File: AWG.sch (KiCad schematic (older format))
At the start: 70 parts, among them J1 Conn Alimenation, J2 Conn afficheur, J3 Conn_01x04, J4 Conn_01x04, J5 SMA, J6 SMA, J7 BNC, Q1 Q_NPN_BCE, Q2 Q_PNP_BCE, SW1 Reset, SW2 Encodeur sur façade, SW3 Next, SW4 Previous, SW5 AC/DC, SW6 50R/Low Z, SW7 Next, SW8 Previous, U1 Pico, U2 L79L05_SOT89, U3 AD8055ARZ, U4 L78L05_SOT89

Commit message: new frontplate interface circuit, new power distrib
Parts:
- removed C1, C11, C2: 100n, Capacitor_SMD:C_0805_2012Metric_Pad1.18x1.45mm_HandSolder, symbol Device:C_Small
- removed C12, C8: 1u, symbol Device:CP_Small
- removed J1: Conn Alimenation, symbol Connector_Generic:Conn_01x04
- removed J3, J4: Conn_01x04, symbol Connector_Generic:Conn_01x04
- removed R1, R14, R15, R2, R3: 1k, Resistor_SMD:R_0805_2012Metric_Pad1.20x1.40mm_HandSolder, symbol Device:R_Small
- removed U2: L79L05_SOT89, Package_TO_SOT_SMD:SOT-89-3, symbol Regulator_Linear:L79L05_SOT89
- removed U4: L78L05_SOT89, Package_TO_SOT_SMD:SOT-89-3, symbol Regulator_Linear:L78L05_SOT89
- added C? (x4): C_Small, symbol Device:C_Small
- added C? (x6): CP_Small, symbol Device:CP_Small
- added C? (x7): 100n, Capacitor_SMD:C_0805_2012Metric_Pad1.18x1.45mm_HandSolder, symbol Device:C_Small
- added J?: Conn_01x03, symbol Connector_Generic:Conn_01x03
- added J?: Conn_01x05, symbol Connector_Generic:Conn_01x05
- added J? (x2): Conn_01x06, symbol Connector_Generic:Conn_01x06
- added R? (x10): 1k, Resistor_SMD:R_0603_1608Metric_Pad0.98x0.95mm_HandSolder, symbol Device:R_Small
- added U?: LM7805, Package_TO_SOT_THT:TO-220-3_Vertical, symbol Regulator_Linear:LM7805_TO220
- added U?: LM7812, Package_TO_SOT_THT:TO-220-3_Vertical, symbol Regulator_Linear:LM7812_TO220
- added U?: LM7905, Package_TO_SOT_THT:TO-220-3_Vertical, symbol Regulator_Linear:LM7905_TO220
- added U?: L7912, symbol Regulator_Linear:L7912
- D1, D2: footprint (none) -> Diode_SMD:D_MELF_Handsoldering
- J2: footprint (none) -> Connector_Molex:Molex_KK-254_AE-6410-10A_1x10_P2.54mm_Vertical
- J5, J6: footprint (none) -> SMA_PINS:SMA_EDGE_NRW
- R10, R11, R12, R13, R16, R17, R18, R19, R20, R21, R22, R23, R24, R25, R26, R27, R28, R30, R31, R32, R33, R34, R35, R4, R5, R6, R7, R8, R9: footprint Resistor_SMD:R_0805_2012Metric_Pad1.20x1.40mm_HandSolder -> Resistor_SMD:R_0603_1608Metric_Pad0.98x0.95mm_HandSolder
- U3: footprint R_8_ADI -> Package_SO:SO-8_3.9x4.9mm_P1.27mm
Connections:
- net labels added: -5V
- wire segments 199 -> 262
- no-connect marks 17 -> 16
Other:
- note added: "To BNC\nand \nswitches"
- note added: "To encoder\n"
- moved on the sheet: C13, C3, C4, C5, C6, C7, C9, D1, D2, J2, J5, J6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

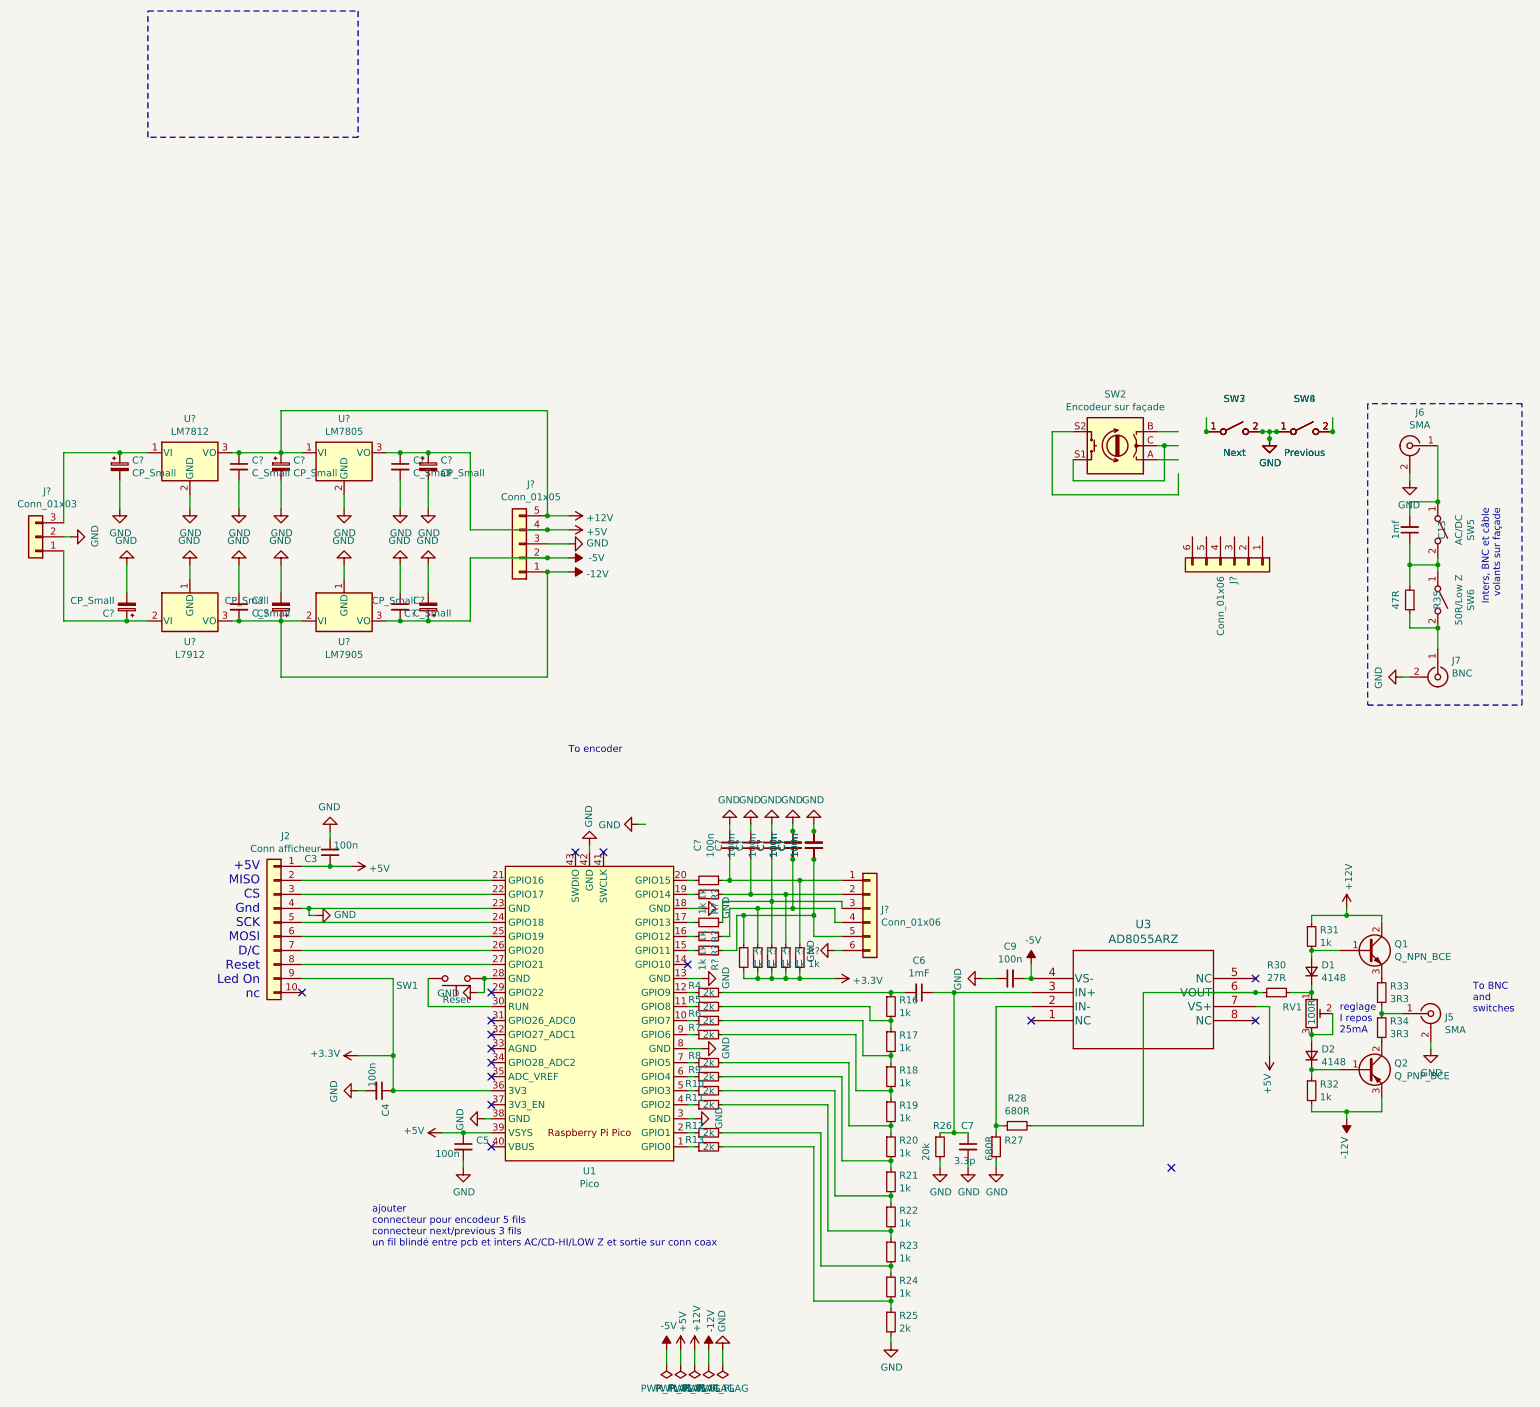
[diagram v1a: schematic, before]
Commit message: interface, power supply &  transistor pinout corrected
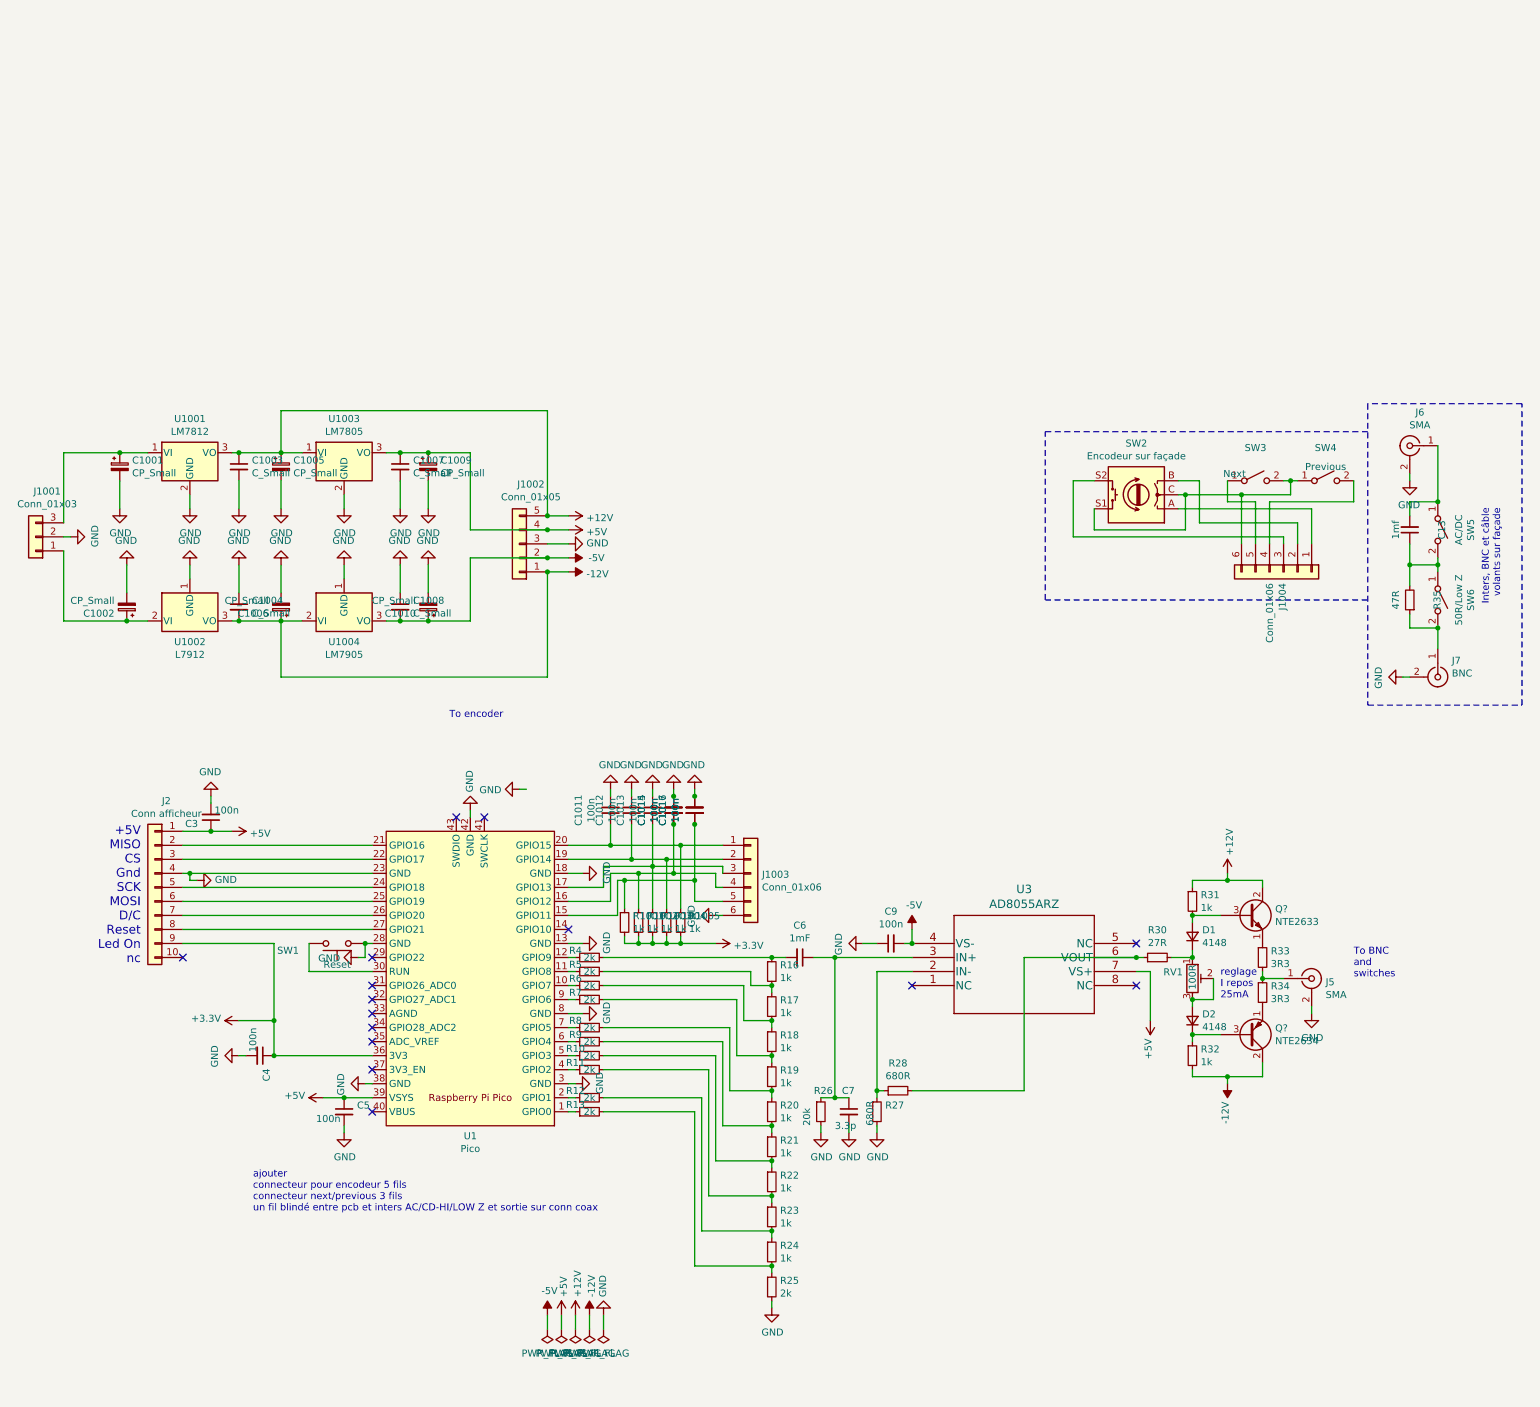
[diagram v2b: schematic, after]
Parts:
- removed Q1: Q_NPN_BCE, symbol Device:Q_NPN_BCE
- removed Q2: Q_PNP_BCE, symbol Device:Q_PNP_BCE
- removed R? (x5): 1k, Resistor_SMD:R_0603_1608Metric_Pad0.98x0.95mm_HandSolder, symbol Device:R_Small
- removed SW7: Next, symbol Switch:SW_SPST
- removed SW8: Previous, symbol Switch:SW_SPST
- added Q?: NTE2633, symbol Device:Q_NPN_ECB
- added Q?: NTE2634, symbol Device:Q_PNP_ECB
- gave numbers to parts that had none: 30
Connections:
- net +12V: now also Q?.2 (C)
- net -12V: now also Q?.2 (C)
- net GND: no longer SW3.2 (B), SW4.1 (A)
- net at U1.15 (GPIO11): now also C1016.1, C1017.1, J1003.5 (Pin_5), R1001.1
- net at U1.16 (GPIO12): now also C1014.1, C1015.1, J1003.4 (Pin_4), R1002.1
- net at U1.17 (GPIO13): now also C1013.1, J1003.3 (Pin_3), R1003.1
- net at U1.19 (GPIO14): now also C1012.1, J1003.2 (Pin_2), R1004.1
- net at U1.20 (GPIO15): now also C1011.1, J1003.1 (Pin_1), R1005.1
- net at SW2.A: now also J1004.1 (Pin_1)
- net at SW2.B: now also J1004.2 (Pin_2)
- net at SW2.C, SW2.S1: now also J1004.6 (Pin_6), SW3.2 (B), SW4.1 (A)
- net at SW2.S2: now also J1004.3 (Pin_3)
- net at SW3.1 (A): now also J1004.5 (Pin_5)
- net at SW4.2 (B): now also J1004.4 (Pin_4)
- net at D2.1 (K), R32.1: now also Q?.3 (B)
- net at D1.2 (A), R31.2: now also Q?.3 (B)
- net at R33.1: now also Q?.1 (E)
- net at R34.2: now also Q?.1 (E)
- no-connect marks 16 -> 15
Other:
- moved on the sheet: C1011, C1012, C1013, C1014, C1015, C1016, C1017, C3, C4, C5, C6, C7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

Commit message: last BOM reference added
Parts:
- C1001, C1002, C1005, C1006, C1009, C1010: value CP_Small -> 100u 50V; footprint (none) -> Capacitor_THT:CP_Radial_D10.0mm_P2.50mm_P5.00mm
- C1003, C1004, C1007, C1008: value C_Small -> 100n; footprint (none) -> Capacitor_SMD:C_0805_2012Metric_Pad1.18x1.45mm_HandSolder
- J1001: footprint (none) -> Connector_Molex:Molex_KK-254_AE-6410-03A_1x03_P2.54mm_Vertical
- J1002: footprint (none) -> Connector_Molex:Molex_KK-254_AE-6410-05A_1x05_P2.54mm_Vertical
- J1003, J1004: footprint (none) -> Connector_Molex:Molex_KK-254_AE-6410-06A_1x06_P2.54mm_Vertical
- Q1001, Q1002: renamed from Q?; footprint (none) -> Package_TO_SOT_THT:TO-220-3_Horizontal_TabDown
- RV1: footprint (none) -> Potentiometer_THT:Potentiometer_Piher_PT-10-V10_Vertical_Hole
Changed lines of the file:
@@
 F 0 "RV1" H 8781 4646 50  0000 R CNN
 F 1 "100R" V 8850 4700 50  0000 R CNN
-F 2 "" H 8850 4600 50  0001 C CNN
+F 2 "Potentiometer_THT:Potentiometer_Piher_PT-10-V10_Vertical_Hole" H 8850 4600 50  0001 C CNN
 F 3 "~" H 8850 4600 50  0001 C CNN
 	1    8850 4600
@@
 F 0 "J1001" H 518 1125 50  0000 C CNN
 F 1 "Conn_01x03" H 518 1216 50  0000 C CNN
-F 2 "" H 600 1450 50  0001 C CNN
+F 2 "Connector_Molex:Molex_KK-254_AE-6410-03A_1x03_P2.54mm_Vertical" H 600 1450 50  0001 C CNN
 F 3 "~" H 600 1450 50  0001 C CNN
 	1    600  1450
@@
 P 3200 950
 F 0 "C1007" H 3292 996 50  0000 L CNN
-F 1 "C_Small" H 3292 905 50  0000 L CNN
-F 2 "" H 3200 950 50  0001 C CNN
+F 1 "100n" H 3292 905 50  0000 L CNN
+F 2 "Capacitor_SMD:C_0805_2012Metric_Pad1.18x1.45mm_HandSolder" H 3200 950 50  0001 C CNN
 F 3 "~" H 3200 950 50  0001 C CNN
 	1    3200 950
@@
 P 3200 1950
 F 0 "C1008" H 3292 1996 50  0000 L CNN
-F 1 "C_Small" H 3292 1905 50  0000 L CNN
-F 2 "" H 3200 1950 50  0001 C CNN
+F 1 "100n" H 3292 1905 50  0000 L CNN
+F 2 "Capacitor_SMD:C_0805_2012Metric_Pad1.18x1.45mm_HandSolder" H 3200 1950 50  0001 C CNN
 F 3 "~" H 3200 1950 50  0001 C CNN
 	1    3200 1950
@@
 P 2050 1950
 F 0 "C1004" H 2142 1996 50  0000 L CNN
-F 1 "C_Small" H 2142 1905 50  0000 L CNN
-F 2 "" H 2050 1950 50  0001 C CNN
+F 1 "100n" H 2142 1905 50  0000 L CNN
+F 2 "Capacitor_SMD:C_0805_2012Metric_Pad1.18x1.45mm_HandSolder" H 2050 1950 50  0001 C CNN
 F 3 "~" H 2050 1950 50  0001 C CNN
 	1    2050 1950
@@
 P 2050 950
 F 0 "C1003" H 2142 996 50  0000 L CNN
-F 1 "C_Small" H 2142 905 50  0000 L CNN
-F 2 "" H 2050 950 50  0001 C CNN
+F 1 "100n" H 2142 905 50  0000 L CNN
+F 2 "Capacitor_SMD:C_0805_2012Metric_Pad1.18x1.45mm_HandSolder" H 2050 950 50  0001 C CNN
 F 3 "~" H 2050 950 50  0001 C CNN
 	1    2050 950
@@
 P 1200 950
 F 0 "C1001" H 1288 996 50  0000 L CNN
-F 1 "CP_Small" H 1288 905 50  0000 L CNN
-F 2 "" H 1200 950 50  0001 C CNN
+F 1 "100u 50V" H 1288 905 50  0000 L CNN
+F 2 "Capacitor_THT:CP_Radial_D10.0mm_P2.50mm_P5.00mm" H 1200 950 50  0001 C CNN
 F 3 "~" H 1200 950 50  0001 C CNN
 	1    1200 950
@@
 P 2350 950
 F 0 "C1005" H 2438 996 50  0000 L CNN
-F 1 "CP_Small" H 2438 905 50  0000 L CNN
-F 2 "" H 2350 950 50  0001 C CNN
+F 1 "100u 50V" H 2438 905 50  0000 L CNN
+F 2 "Capacitor_THT:CP_Radial_D10.0mm_P2.50mm_P5.00mm" H 2350 950 50  0001 C CNN
 F 3 "~" H 2350 950 50  0001 C CNN
 	1    2350 950
@@
 P 1250 1950
 F 0 "C1002" H 1338 1996 50  0000 L CNN
-F 1 "CP_Small" H 1338 1905 50  0000 L CNN
-F 2 "" H 1250 1950 50  0001 C CNN
+F 1 "100u 50V" H 1338 1905 50  0000 L CNN
+F 2 "Capacitor_THT:CP_Radial_D10.0mm_P2.50mm_P5.00mm" H 1250 1950 50  0001 C CNN
 F 3 "~" H 1250 1950 50  0001 C CNN
 	1    1250 1950
@@
 P 2350 1950
 F 0 "C1006" H 2438 1996 50  0000 L CNN
-F 1 "CP_Small" H 2438 1905 50  0000 L CNN
-F 2 "" H 2350 1950 50  0001 C CNN
+F 1 "100u 50V" H 2438 1905 50  0000 L CNN
+F 2 "Capacitor_THT:CP_Radial_D10.0mm_P2.50mm_P5.00mm" H 2350 1950 50  0001 C CNN
 F 3 "~" H 2350 1950 50  0001 C CNN
 	1    2350 1950
@@
 P 3400 950
 F 0 "C1009" H 3488 996 50  0000 L CNN
-F 1 "CP_Small" H 3488 905 50  0000 L CNN
-F 2 "" H 3400 950 50  0001 C CNN
+F 1 "100u 50V" H 3488 905 50  0000 L CNN
+F 2 "Capacitor_THT:CP_Radial_D10.0mm_P2.50mm_P5.00mm" H 3400 950 50  0001 C CNN
 F 3 "~" H 3400 950 50  0001 C CNN
 	1    3400 950
@@
 P 3400 1950
 F 0 "C1010" H 3488 1996 50  0000 L CNN
-F 1 "CP_Small" H 3488 1905 50  0000 L CNN
-F 2 "" H 3400 1950 50  0001 C CNN
+F 1 "100u 50V" H 3488 1905 50  0000 L CNN
+F 2 "Capacitor_THT:CP_Radial_D10.0mm_P2.50mm_P5.00mm" H 3400 1950 50  0001 C CNN
 F 3 "~" H 3400 1950 50  0001 C CNN
 	1    3400 1950
@@
 F 0 "J1002" H 3968 1075 50  0000 C CNN
 F 1 "Conn_01x05" H 3968 1166 50  0000 C CNN
-F 2 "" H 4050 1500 50  0001 C CNN
+F 2 "Connector_Molex:Molex_KK-254_AE-6410-05A_1x05_P2.54mm_Vertical" H 4050 1500 50  0001 C CNN
 F 3 "~" H 4050 1500 50  0001 C CNN
 	1    4050 1500
@@
 F 0 "J1003" H 5780 3842 50  0000 L CNN
 F 1 "Conn_01x06" H 5780 3751 50  0000 L CNN
-F 2 "" H 5700 3850 50  0001 C CNN
+F 2 "Connector_Molex:Molex_KK-254_AE-6410-06A_1x06_P2.54mm_Vertical" H 5700 3850 50  0001 C CNN
 F 3 "~" H 5700 3850 50  0001 C CNN
 	1    5700 3850
@@
 F 0 "J1004" H 9580 1692 50  0000 L CNN
 F 1 "Conn_01x06" H 9580 1601 50  0000 L CNN
-F 2 "" H 9500 1700 50  0001 C CNN
+F 2 "Connector_Molex:Molex_KK-254_AE-6410-06A_1x06_P2.54mm_Vertical" H 9500 1700 50  0001 C CNN
 F 3 "~" H 9500 1700 50  0001 C CNN
 	1    9500 1700
@@
 	7800 700  10100 700
 $Comp
-L Device:Q_NPN_ECB Q?
+L Device:Q_NPN_ECB Q1001
 U 1 1 61CFB742
 P 9250 4150
-F 0 "Q?" H 9440 4196 50  0000 L CNN
+F 0 "Q1001" H 9440 4196 50  0000 L CNN
 F 1 "NTE2633" H 9440 4105 50  0000 L CNN
-F 2 "" H 9450 4250 50  0001 C CNN
+F 2 "Package_TO_SOT_THT:TO-220-3_Horizontal_TabDown" H 9450 4250 50  0001 C CNN
 F 3 "~" H 9250 4150 50  0001 C CNN
 	1    9250 4150
@@
 $EndComp
 $Comp
-L Device:Q_PNP_ECB Q?
+L Device:Q_PNP_ECB Q1002
 U 1 1 61CFC7DE
 P 9250 5000
-F 0 "Q?" H 9440 4954 50  0000 L CNN
+F 0 "Q1002" H 9440 4954 50  0000 L CNN
 F 1 "NTE2634" H 9440 5045 50  0000 L CNN
-F 2 "" H 9450 5100 50  0001 C CNN
+F 2 "Package_TO_SOT_THT:TO-220-3_Horizontal_TabDown" H 9450 5100 50  0001 C CNN
 F 3 "~" H 9250 5000 50  0001 C CNN
 	1    9250 5000
